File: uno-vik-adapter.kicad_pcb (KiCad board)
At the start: 2 copper layers, 68.6 x 53.3 mm, 15 parts, among them J1 Power, J2 Digital/PWM, J3 Analog, J4 Digital/PWM

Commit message: Tweaks to refs.
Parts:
- renumbered REF** to VMH1, REF** to VMH2, REF** to VMH3
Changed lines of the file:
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@@
 		(layer "F.Cu")
 		(at 134.25 73.33 90)
-		(property "Reference" "REF**"
+		(property "Reference" "VMH1"
 			(at 0 -0.5 90)
 			(unlocked yes)
@@
 		(descr "Mounting Hole 2.2mm, M2")
 		(tags "mounting hole 2.2mm m2")
-		(property "Reference" "REF**"
+		(property "Reference" "VMH3"
 			(at 0 -7.85 0)
 			(layer "F.SilkS")
@@
 		(descr "Mounting Hole 2.2mm, M2")
 		(tags "mounting hole 2.2mm m2")
-		(property "Reference" "REF**"
+		(property "Reference" "VMH2"
 			(at 0 -3.2 0)
 			(layer "F.SilkS")

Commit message: Tweaks.
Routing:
- net /TX/1: track 89.1 -> 105.5 mm
- net /GP_AD1: track 72.8 -> 78.0 mm
- net /RX/0: track 96.9 -> 99.1 mm
- net /GP_AD2: track 59.7 -> 60.5 mm

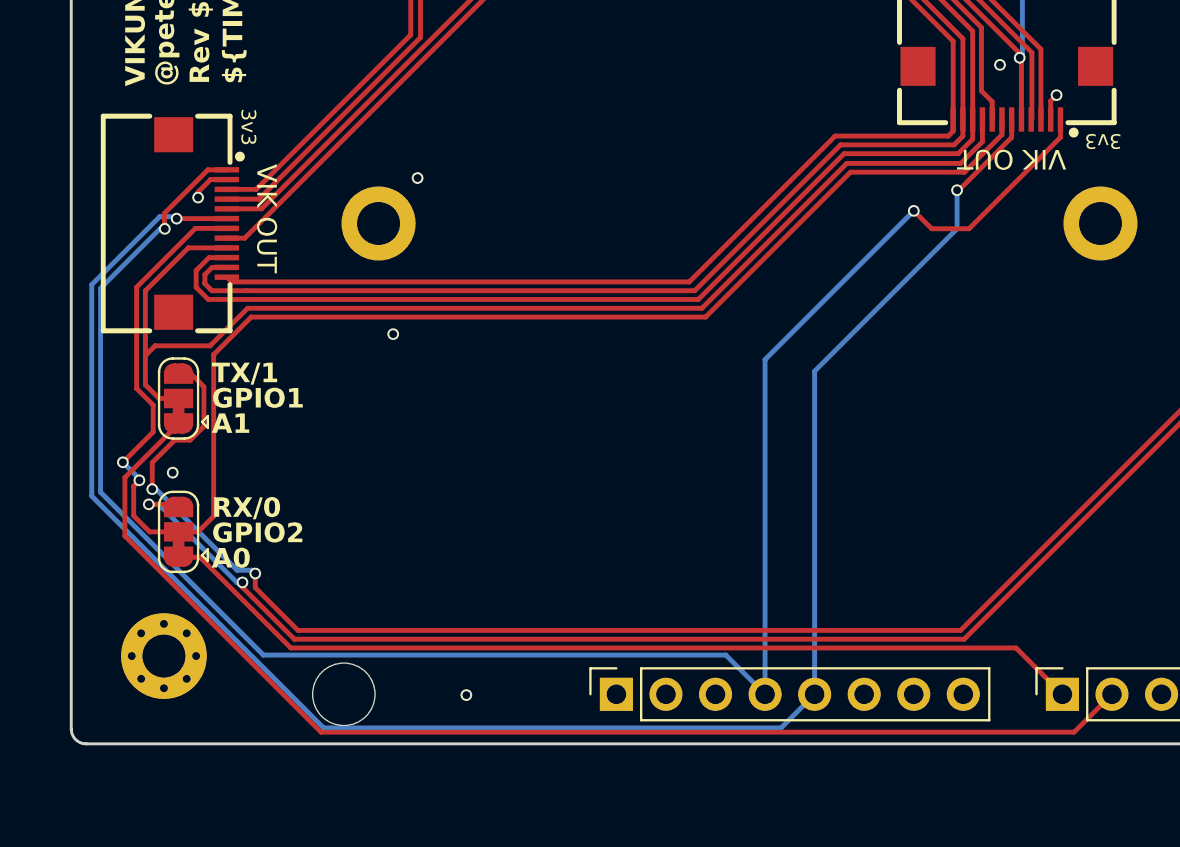
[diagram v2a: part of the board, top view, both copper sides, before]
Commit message: Add jumpers for 5v pin.
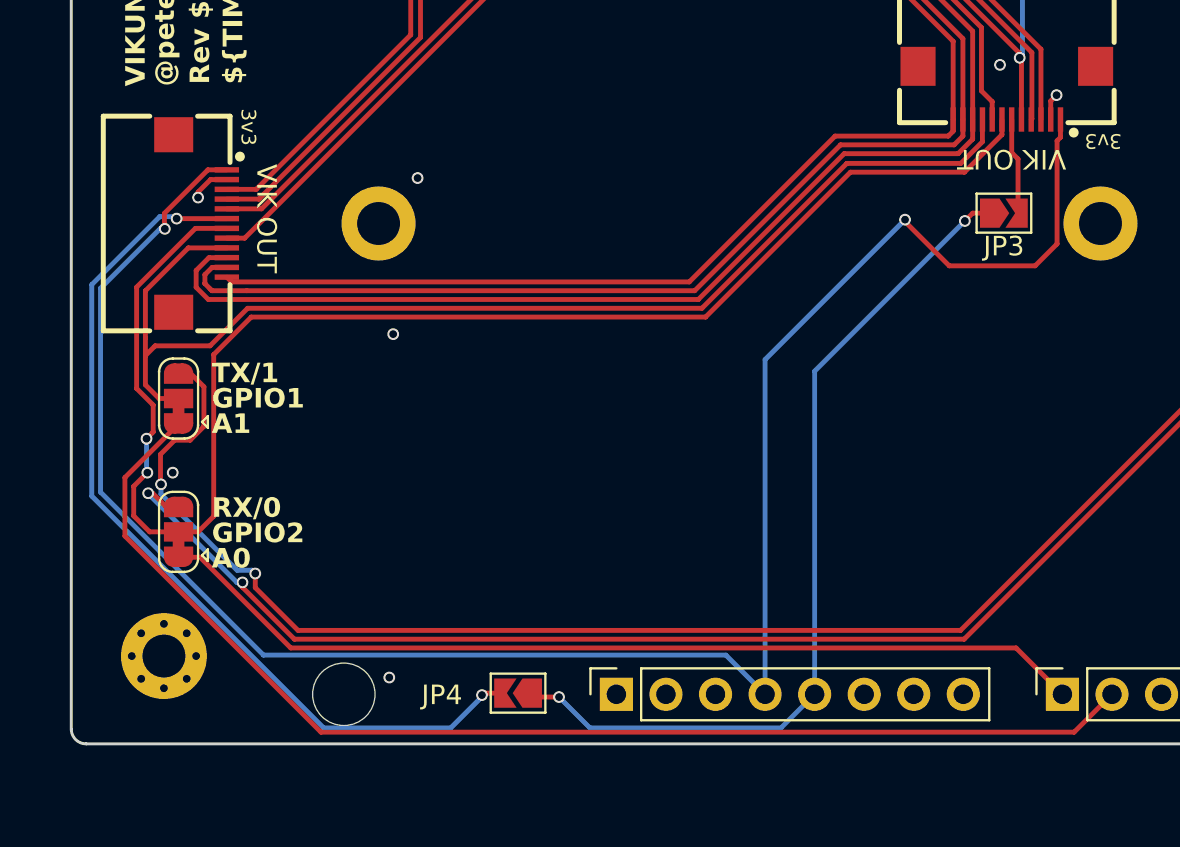
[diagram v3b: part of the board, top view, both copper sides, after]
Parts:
- added JP3: SolderJumper_2_Open, Jumper:SolderJumper-2_P1.3mm_Open_TrianglePad1.0x1.5mm, F.Cu at (147.8, 72.8)
- added JP4: SolderJumper_2_Open, Jumper:SolderJumper-2_P1.3mm_Open_TrianglePad1.0x1.5mm, F.Cu at (122.9, 97.4)
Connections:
- J5 pad 6: +5V -> Net-(J5-5V)
- J6 pad 6: +5V -> Net-(J6-5V)
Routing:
- net +5V: track 95.6 -> 44.8 mm
- net Net-(J6-5V): track 0.00 -> 46.1 mm, vias 0 -> 2
- net Net-(J5-5V): track 0.00 -> 4.93 mm
- net +3V3: track 97.0 -> 101.3 mm
- net /GP_AD1: track 78.0 -> 77.3 mm
- net /RX/0: track 99.1 -> 99.7 mm
